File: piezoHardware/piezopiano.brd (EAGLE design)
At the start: 90 x 99.8 mm, 46 parts, among them J1 CON2, Q1 BSS123, Q2 BSS123, Q3 BSS123, Q4 BSS123, Q5 BSS123, Q6 BSS123, Q7 BSS123, Q8 BSS123, U1 MEGA328PB-AU

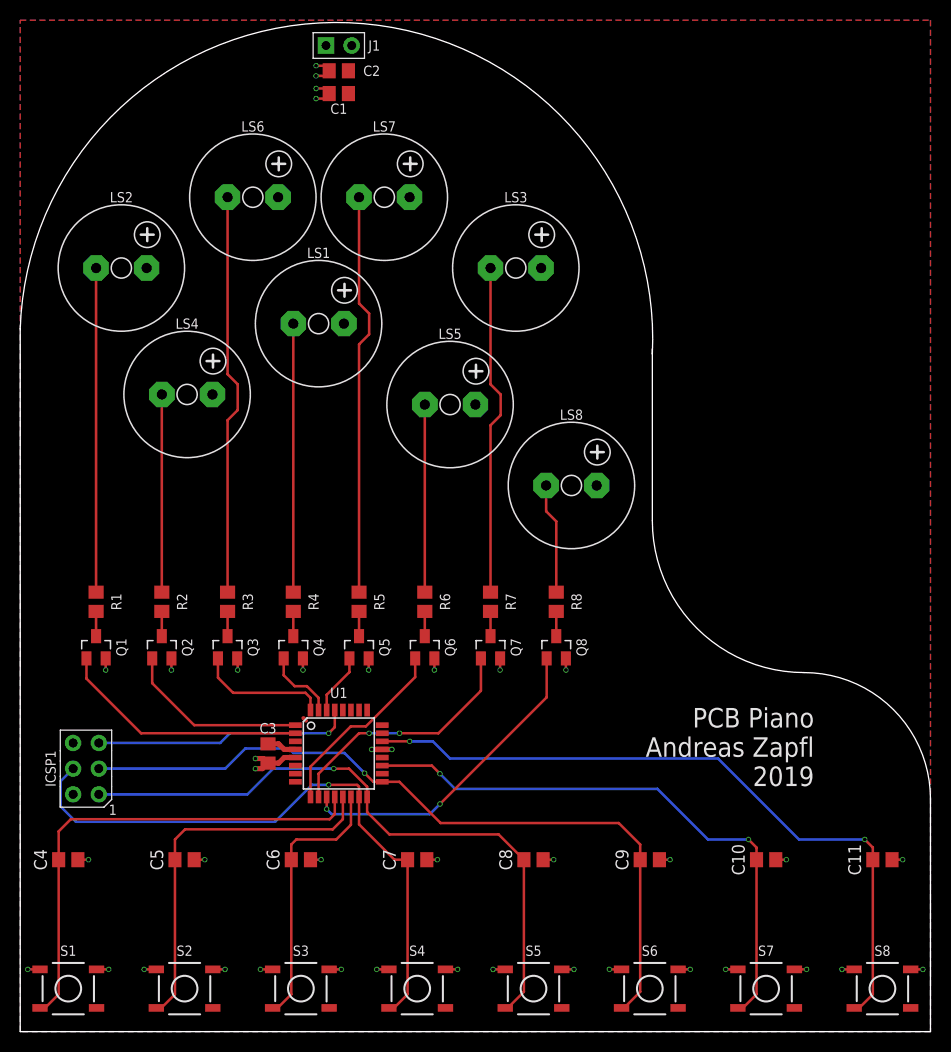
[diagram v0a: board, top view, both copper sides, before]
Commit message: LDO added
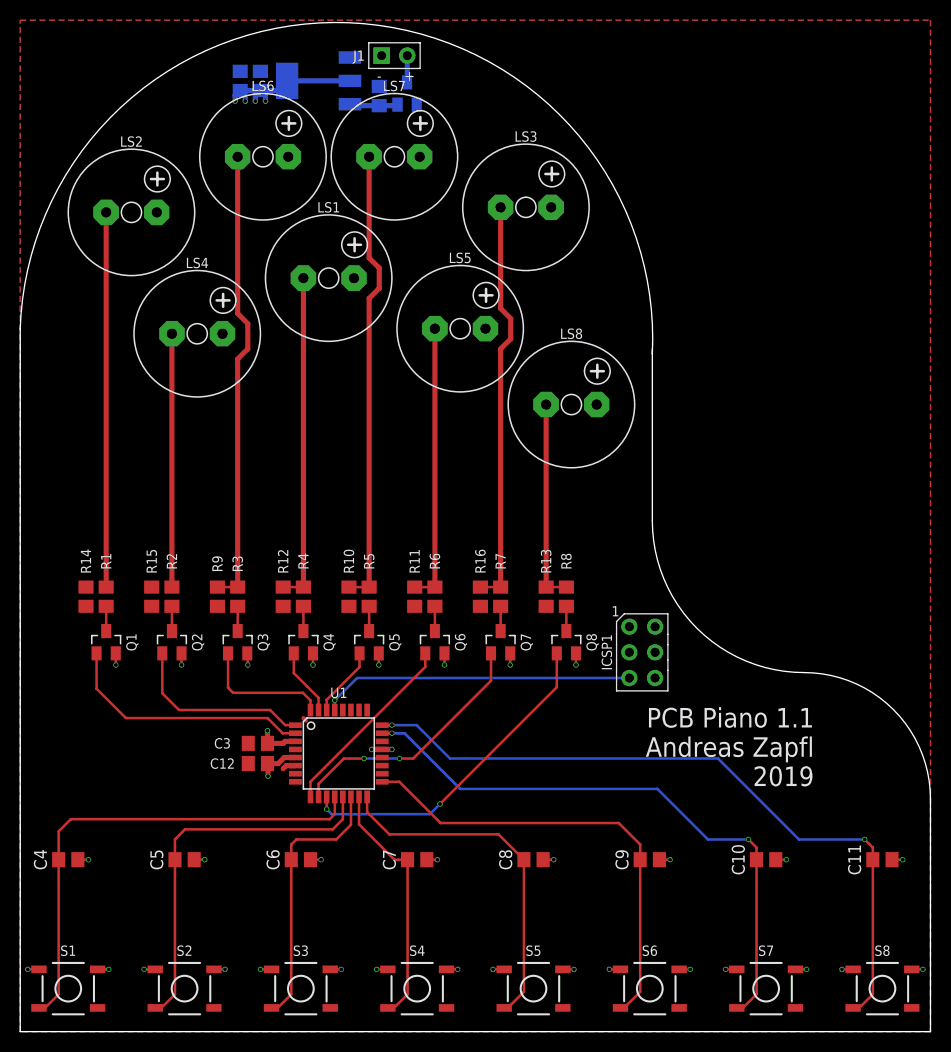
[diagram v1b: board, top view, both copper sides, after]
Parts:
- added C12: 100n, zaan-Capacitors:C0805
- added C13: 10u, zaan-Capacitors:C0805
- added Q9: DMP3099L, zaan-Discrete:SOT23
- added R10, R11, R12, R13, R14, R15, R16, R9: 10k, zaan-Resistors:R0805
- added U2: AZ1117H-5.0TRE1, zaan-IC-Power:SOT223
- C1, C10, C11, C3, C4, C5, C6, C7, C8, C9: device rcl:C0805 -> zaan-Capacitors:C0805
- C2: value 100n -> 4.7u; device rcl:C0805 -> zaan-Capacitors:C0805
- LS1, LS2, LS3, LS4, LS5, LS6, LS7, LS8: device Custom:F/CM12P -> zaan-Electromechanical:CM12P/5.0P
- Q1, Q2, Q3, Q4, Q5, Q6, Q7, Q8: value BSS123 -> DMN3404L; device Custom:SOT23 -> zaan-Discrete:SOT23
- R1, R2, R3, R4, R5, R6, R7, R8: value (none) -> 100R; device rcl:R0805 -> zaan-Resistors:R0805
- S1, S2, S3, S4, S5, S6, S7, S8: device Custom:TACTILE_SWITCH_SMD_5.2MM -> zaan-Electromechanical:TACTILE_SWITCH_SMD_5.2MM
- U1: value MEGA328PB-AU -> MEGA48A-AU; device Custom:TQFP32-08 -> zaan-IC-Microcontroller:TQFP32-08
- moved ICSP1 56.2 mm to (61.5, 37.5), turned to 0 degrees
- moved C1 9.83 mm to (21.8, 94.0), flipped to the bottom, turned to 90 degrees
- moved LS8 8.00 mm to (54.5, 62.0)
- moved LS5 7.57 mm to (43.5, 69.5)
- moved LS3 6.08 mm to (50.0, 81.5)
- moved LS4 6.08 mm to (17.5, 69.0)
- moved J1 5.59 mm to (37.0, 96.5)
- moved LS2 5.59 mm to (11.0, 81.0)
- moved C2 4.72 mm to (35.5, 92.5), flipped to the bottom, turned to 90 degrees
- moved LS1 4.61 mm to (30.5, 74.5)
- moved LS6 4.12 mm to (24.0, 86.5)
- moved LS7 4.12 mm to (37.0, 86.5)
- moved C3 1.41 mm to (23.5, 28.5), turned to 0 degrees
- moved Q1 1.12 mm to (8.50, 38.5)
- moved Q2 1.12 mm to (15.0, 38.5)
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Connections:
- new net N$17: C2.1, Q9.2, U2.3
- new net N$18: LS6.-, R3.2, R9.1
- net +5V: now also C12.1, C13.1, R10.2, R11.2, R12.2, R13.2, R14.2, R15.2, R16.2, R9.2, U1.6, U2.2, U2.4; no longer C2.1, J1.2
- net GND: now also C12.2, C13.2, Q9.1, U1.3, U2.1
- net N$1: now also J1.2, Q9.3; no longer LS6.-, R3.2
- net N$10: now also R12.1
- net N$11: now also R14.1
- net N$13: now also R10.1
- net N$15: now also R13.1
- net N$16: now also R16.1
- net N$4: now also R15.1
- net N$6: now also R11.1
- net T5: now also U1.24; no longer U1.22
- net T6: now also U1.23; no longer U1.19
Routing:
- net N$18: track 0.00 -> 45.4 mm
- net N$1: track 39.9 -> 2.66 mm
- net T1: track 61.6 -> 24.8 mm, vias 1 -> 0
- net T7: track 75.4 -> 45.2 mm, vias 1 -> 0
- net T8: track 63.8 -> 34.6 mm, vias 1 -> 0
- net +5V: track 3.29 -> 18.3 mm, vias 0 -> 4
- net N$15: track 11.0 -> 20.0 mm
- net N$6: track 18.5 -> 27.5 mm
- net N$16: track 32.9 -> 40.4 mm
- net N$10: track 26.5 -> 32.5 mm
- net N$4: track 19.5 -> 25.0 mm
- net N$13: track 39.9 -> 45.4 mm
- net RST: track 25.7 -> 31.0 mm
- net N$11: track 32.0 -> 37.0 mm
- net N$17: track 0.00 -> 4.80 mm
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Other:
- board text added: "+"
- board text added: "-"
- board text added: "PCB Piano 1.1 Andreas Zapfl 2019"

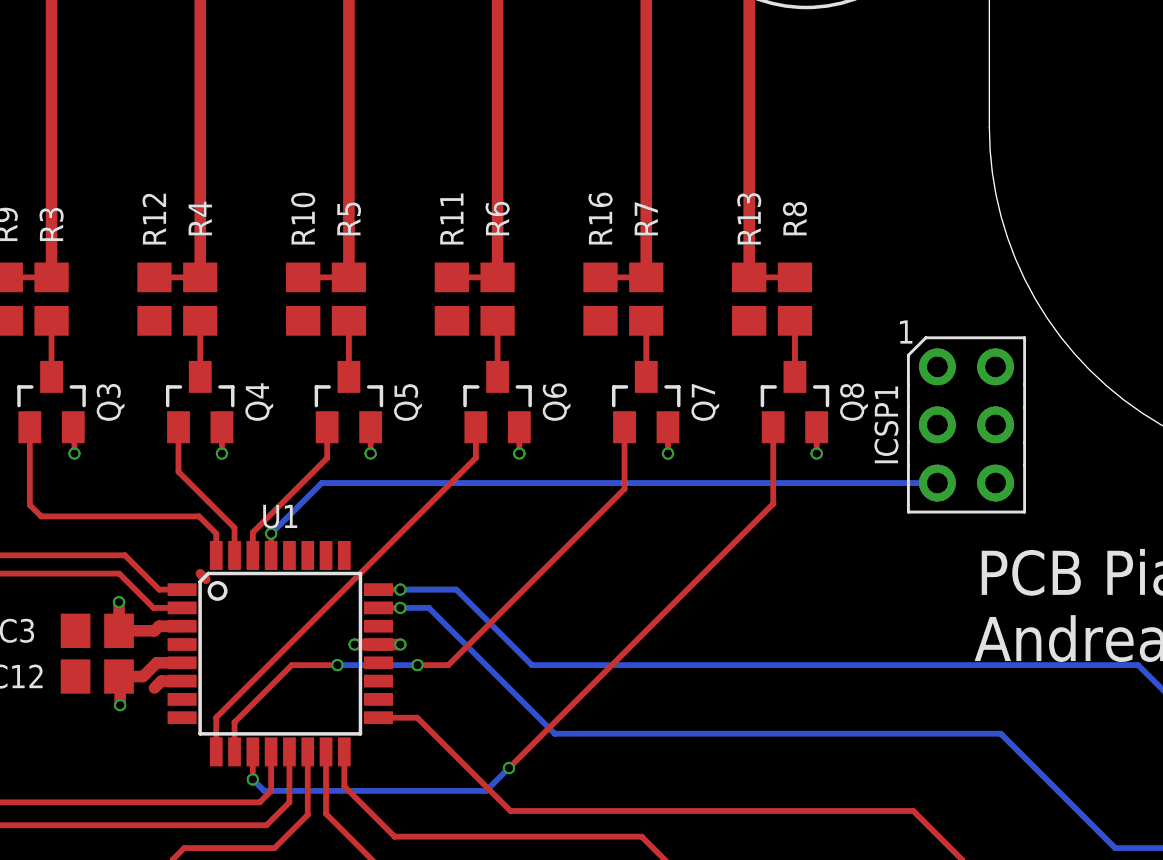
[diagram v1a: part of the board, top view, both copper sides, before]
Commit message: ATmega silkscreen change
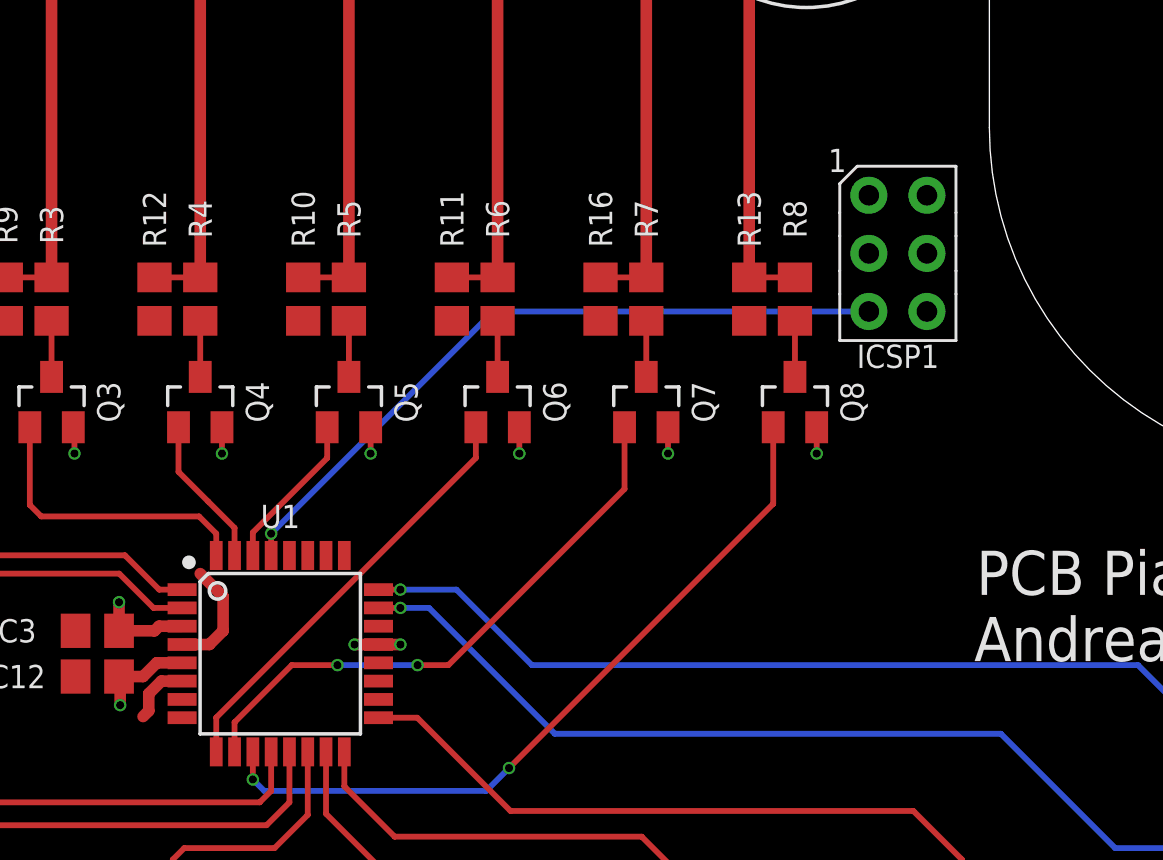
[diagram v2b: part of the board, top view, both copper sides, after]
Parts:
- moved ICSP1 8.08 mm to (58.5, 45.0)
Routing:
- net +5V: track 18.3 -> 24.4 mm
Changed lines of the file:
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@@
 <attribute name="VOLTAGE" value="50V" x="50.75" y="17" size="1.778" layer="27" display="off"/>
 </element>
-<element name="ICSP1" library="Custom" package="AVRISP-2.54" value="AVRISP2.54MM" x="61.5" y="37.5" smashed="yes">
-<attribute name="NAME" x="58" y="37.5" size="1.016" layer="25" font="vector" ratio="15" rot="R270" align="center"/>
+<element name="ICSP1" library="Custom" package="AVRISP-2.54" value="AVRISP2.54MM" x="58.5" y="45" smashed="yes">
+<attribute name="NAME" x="58.5" y="40.5" size="1.016" layer="25" font="vector" ratio="15" align="center"/>
 </element>
 <element name="J1" library="Custom" package="H2-2.54" value="CON2" x="37" y="96.5" smashed="yes" rot="R90">
@@
 <contactref element="ICSP1" pad="2"/>
 <contactref element="U1" pad="18"/>
-<wire x1="28" y1="31" x2="28.25" y2="30.75" width="0.4064" layer="1"/>
 <contactref element="R9" pad="2"/>
 <contactref element="R10" pad="2"/>
@@
 <contactref element="C12" pad="1"/>
 <wire x1="27.2074" y1="26.3" x2="26.3" y2="26.3" width="0.508" layer="1"/>
-<wire x1="26.3" y1="26.3" x2="26" y2="26" width="0.508" layer="1"/>
 <contactref element="U2" pad="4"/>
 <contactref element="U2" pad="2"/>
@@
 <wire x1="26.401" y1="93.401" x2="26.401" y2="94" width="0.508" layer="16"/>
 <wire x1="26.401" y1="94" x2="32.599" y2="94" width="0.508" layer="16"/>
-<wire x1="27.2074" y1="27.9" x2="28.25" y2="30.75" width="0" layer="19" extent="1-1"/>
-<wire x1="22.55" y1="26.5" x2="26" y2="26" width="0" layer="19" extent="1-1"/>
+<wire x1="27.2074" y1="27.9" x2="28.4" y2="27.9" width="0.508" layer="1"/>
+<wire x1="28.4" y1="27.9" x2="29" y2="28.5" width="0.508" layer="1"/>
+<wire x1="29" y1="28.5" x2="29" y2="30" width="0.508" layer="1"/>
+<wire x1="29" y1="30" x2="28" y2="31" width="0.508" layer="1"/>
+<wire x1="25.75" y1="25" x2="25.5" y2="24.75" width="0.508" layer="1"/>
+<wire x1="26.3" y1="26.3" x2="25.75" y2="25.75" width="0.508" layer="1"/>
+<wire x1="25.75" y1="25.75" x2="25.75" y2="25" width="0.508" layer="1"/>
 </signal>
 <signal name="N$2">
@@
 <wire x1="37" y1="17" x2="38.3" y2="17" width="0.254" layer="1"/>
 <contactref element="ICSP1" pad="4"/>
-<wire x1="38.3" y1="17" x2="62.77" y2="37.5" width="0" layer="19" extent="1-1"/>
+<wire x1="33.5" y1="23.2074" x2="59.77" y2="45" width="0" layer="19" extent="1-1"/>
 <wire x1="42.15" y1="2.345" x2="38.3" y2="3.689" width="0" layer="19" extent="1-1"/>
 </signal>
@@
 <wire x1="37.48755" y1="24.7" x2="41.56455" y2="20.623" width="0.254" layer="1"/>
 <contactref element="ICSP1" pad="3"/>
-<wire x1="59.177" y1="20.623" x2="60.23" y2="37.5" width="0" layer="19" extent="1-1"/>
+<wire x1="59.177" y1="20.623" x2="57.23" y2="45" width="0" layer="19" extent="1-1"/>
 <wire x1="65.15" y1="2.345" x2="61.3" y2="3.939" width="0" layer="19" extent="1-1"/>
 </signal>
@@
 <wire x1="36.5" y1="19.5" x2="47.3" y2="19.5" width="0.254" layer="1"/>
 <contactref element="ICSP1" pad="1"/>
-<wire x1="47.3" y1="19.5" x2="60.23" y2="40.04" width="0" layer="19" extent="1-1"/>
+<wire x1="47.3" y1="19.5" x2="57.23" y2="47.54" width="0" layer="19" extent="1-1"/>
 <wire x1="53.65" y1="2.345" x2="49.8" y2="3.939" width="0" layer="19" extent="1-1"/>
 </signal>
@@
 <wire x1="31.1" y1="31.7926" x2="31.1" y2="32.75" width="0.254" layer="1"/>
 <via x="31.1" y="32.75" extent="1-16" drill="0.35"/>
-<wire x1="31.1" y1="32.75" x2="33.31" y2="34.96" width="0.254" layer="16"/>
-<wire x1="33.31" y1="34.96" x2="60.23" y2="34.96" width="0.254" layer="16"/>
+<wire x1="31.1" y1="32.75" x2="40.81" y2="42.46" width="0.254" layer="16"/>
+<wire x1="40.81" y1="42.46" x2="57.23" y2="42.46" width="0.254" layer="16"/>
 </signal>
 <signal name="N$18">

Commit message: Partly finished layout
Missing crystal
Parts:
- removed C11, C12: 100n, zaan-Capacitors:C0805
- removed C13: 10u, zaan-Capacitors:C0805
- removed Q9: DMP3099L, zaan-Discrete:SOT23
- removed U2: AZ1117H-5.0TRE1, zaan-IC-Power:SOT223
- added C100: 4.7u, zaan-Capacitors:C0805
- added C101: 10u, zaan-Capacitors:C0805
- added C102: 100n, zaan-Capacitors:C0805
- added Q100: DMP3099L, zaan-Discrete:SOT23
- added U100: AZ1117H-5.0TRE1, zaan-IC-Power:SOT223
- C2: value 4.7u -> 100n
- R1, R3, R5, R7: value 100R -> 10k
- R10, R12, R14, R16: value 10k -> 100R
- moved C2 67.1 mm to (23.5, 26.5), flipped to the top, turned to 0 degrees
- moved C1 65.5 mm to (23.5, 28.5), flipped to the top, turned to 0 degrees
- moved R14 41.0 mm to (47.5, 43.0), turned to 90 degrees
- moved R15 39.0 mm to (52.0, 43.0)
- moved LS4 37.8 mm to (54.5, 61.5)
- moved LS5 34.3 mm to (11.0, 80.5)
- moved ICSP1 30.5 mm to (82.0, 25.5)
- moved LS8 29.7 mm to (37.0, 86.0)
- moved LS6 26.6 mm to (50.0, 81.0)
- moved R8 26.0 mm to (28.0, 43.0)
- moved C3 22.0 mm to (4.75, 17.0)
- moved R7 21.5 mm to (26.0, 43.0), turned to 270 degrees
- moved LS3 20.9 mm to (30.5, 74.0)
- moved R6 19.5 mm to (21.5, 43.0)
- moved R12 15.0 mm to (41.0, 43.0), turned to 90 degrees
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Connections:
- net +5V: now also C101.1, C102.1, C2.1, R1.2, R3.2, R5.2, R7.2, U100.2, U100.4; no longer C12.1, C13.1, C3.1, R10.2, R12.2, R14.2, R16.2, U2.2, U2.4
- net GND: now also C100.2, C101.2, C102.2, Q100.1, U100.1; no longer C11.2, C12.2, C13.2, Q9.1, U2.1
- net N$1: now also Q100.3; no longer Q9.3
- net N$10: now also LS3.-, R7.1, R8.2; no longer LS1.-, R12.1, R4.2
- net N$11: now also LS5.-, R1.1, R2.2; no longer LS2.-, R1.2, R14.1
- net N$12: now also R4.1; no longer R2.1
- net N$13: now also LS8.-, R10.2, R9.1; no longer LS7.-, R10.1, R5.2
- net N$14: now also R12.1; no longer R6.1
- net N$15: now also LS4.-, R15.1, R16.2; no longer LS8.-, R13.1, R8.2
- net N$16: now also LS6.-, R13.1, R14.2; no longer LS3.-, R16.1, R7.2
- net N$17: now also C100.1, Q100.2, U100.3; no longer C2.1, Q9.2, U2.3
- net N$18: now also LS7.-, R5.1, R6.2; no longer LS6.-, R3.2, R9.1
- net N$2: now also R8.1; no longer R4.1
- net N$3: now also R2.1; no longer R1.1
- net N$4: now also LS2.-, R3.1, R4.2; no longer LS4.-, R15.1, R2.2
- net N$5: now also R10.1; no longer R5.1
- net N$6: now also LS1.-, R12.2; no longer LS5.-, R6.2
- net N$7: now also R16.1; no longer R8.1
- net N$8: now also R14.1; no longer R7.1
- net N$9: now also R6.1; no longer R3.1
- net T1: now also C6.1; no longer C7.1
- net T2: now also C5.1; no longer C6.1
- net T3: now also C4.1; no longer C5.1
- net T4: now also C3.1; no longer C4.1
- net T5: now also C10.1; no longer C11.1
- net T6: now also C9.1; no longer C10.1
- net T7: now also C8.1; no longer C9.1
- net T8: now also C7.1; no longer C8.1
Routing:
- net T1: track 24.8 -> 77.3 mm, vias 0 -> 2
- net T8: track 34.6 -> 84.5 mm, vias 0 -> 2
- net RST: track 31.1 -> 54.7 mm
- net T7: track 45.2 -> 67.5 mm
- net GND: track 47.7 -> 45.6 mm
- net N$4: track 25.0 -> 26.5 mm
- net N$11: track 37.0 -> 38.5 mm
- net NOTE7: track 32.7 -> 33.6 mm
- net N$6: track 27.5 -> 27.0 mm
- net N$18: track 45.4 -> 44.9 mm
- net N$16: track 40.4 -> 39.9 mm
- net N$15: track 20.0 -> 19.5 mm
- net N$13: track 45.4 -> 44.9 mm
- net N$10: track 32.5 -> 32.0 mm
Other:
- board text removed: "PCB Piano Andreas Zapfl 2019"

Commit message: Minor part update
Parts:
- U100: value AZ1117H-5.0TRE1 -> AP7381-50Y-13; device zaan-IC-Power:SOT223 -> zaan-IC-Power:SOT89
- moved C102 3.50 mm to (25.2, 93.5), turned to 270 degrees
- moved C101 0.50 mm to (23.2, 93.5), turned to 270 degrees
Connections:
- net +5V: now also U100.1; no longer U100.2, U100.4
- net GND: now also U100.2, U100.2@1; no longer U100.1
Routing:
- net +5V: track 24.4 -> 19.7 mm, vias 4 -> 2
- net N$17: track 4.80 -> 6.25 mm
